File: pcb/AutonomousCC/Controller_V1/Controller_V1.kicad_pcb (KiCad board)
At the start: 2 copper layers, 7 parts, among them J1 Antenna_Conn_02x04_Odd_Even, U1 COM-09032, U2 Pico, U3 COM-09032

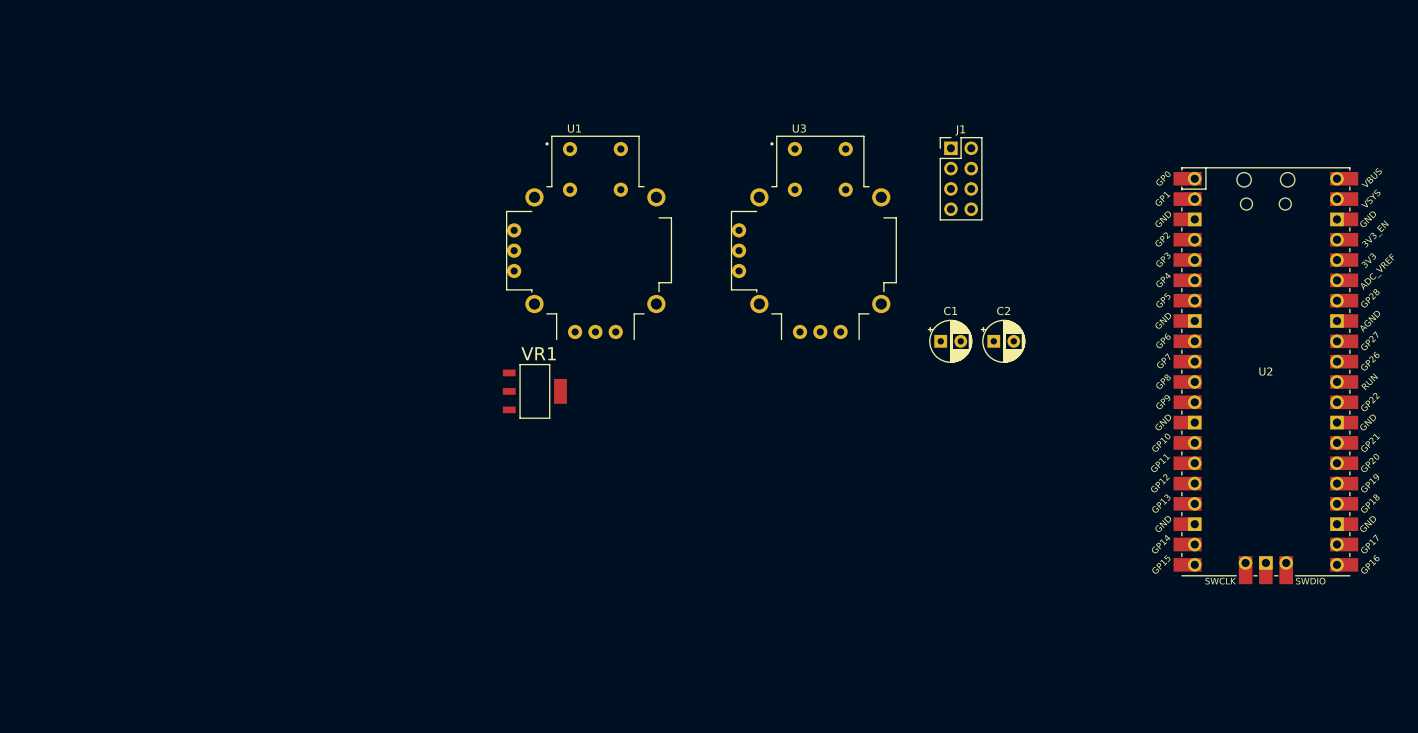
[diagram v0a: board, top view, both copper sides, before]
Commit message: Added USB Port, Button, LED
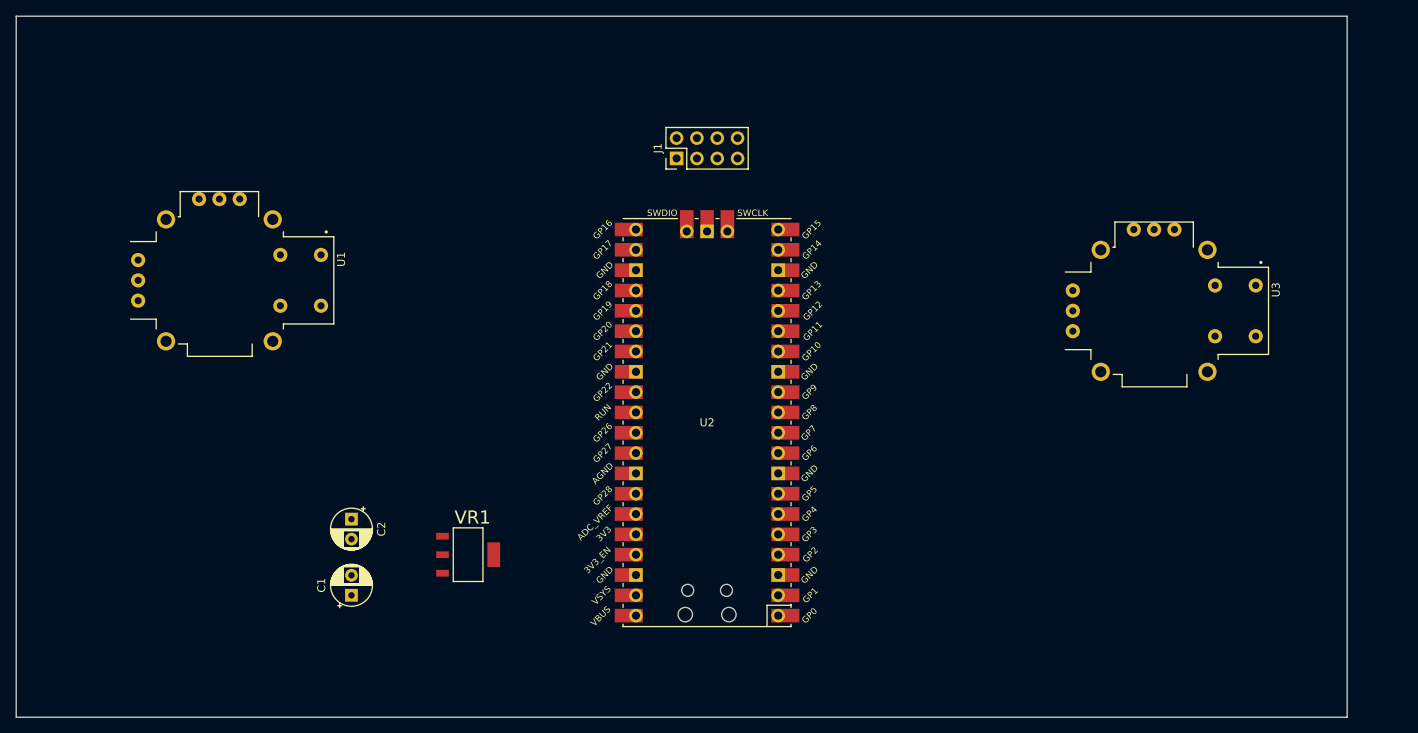
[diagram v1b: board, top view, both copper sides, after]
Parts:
- moved C2 83.3 mm to (118.1, 113.7), turned to 270 degrees
- moved C1 80.2 mm to (118.1, 123.2), turned to 90 degrees
- moved U2 70.1 mm to (162.6, 101.6), turned to 180 degrees
- moved U1 47.2 mm to (101.6, 83.8), turned to 270 degrees
- moved U3 42.4 mm to (218.4, 87.6), turned to 270 degrees
- moved J1 34.3 mm to (158.8, 68.6), turned to 90 degrees
- moved VR1 22.1 mm to (132.7, 118.1)
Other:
- board outline added: 166.4 x 87.6 mm

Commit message: Updated Sch
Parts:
- added J2: USB1130-15-A_REVA, MCU_RaspberryPi_and_Boards:GCT_USB1130-15-A_REVA, F.Cu at (229.9, 61.0)
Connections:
- net Net-(U2-Pad12) renamed GP09
- net Net-(U2-Pad14) renamed GP10
- net Net-(U2-Pad20) renamed GP15
- net Net-(U2-Pad21) renamed GP16

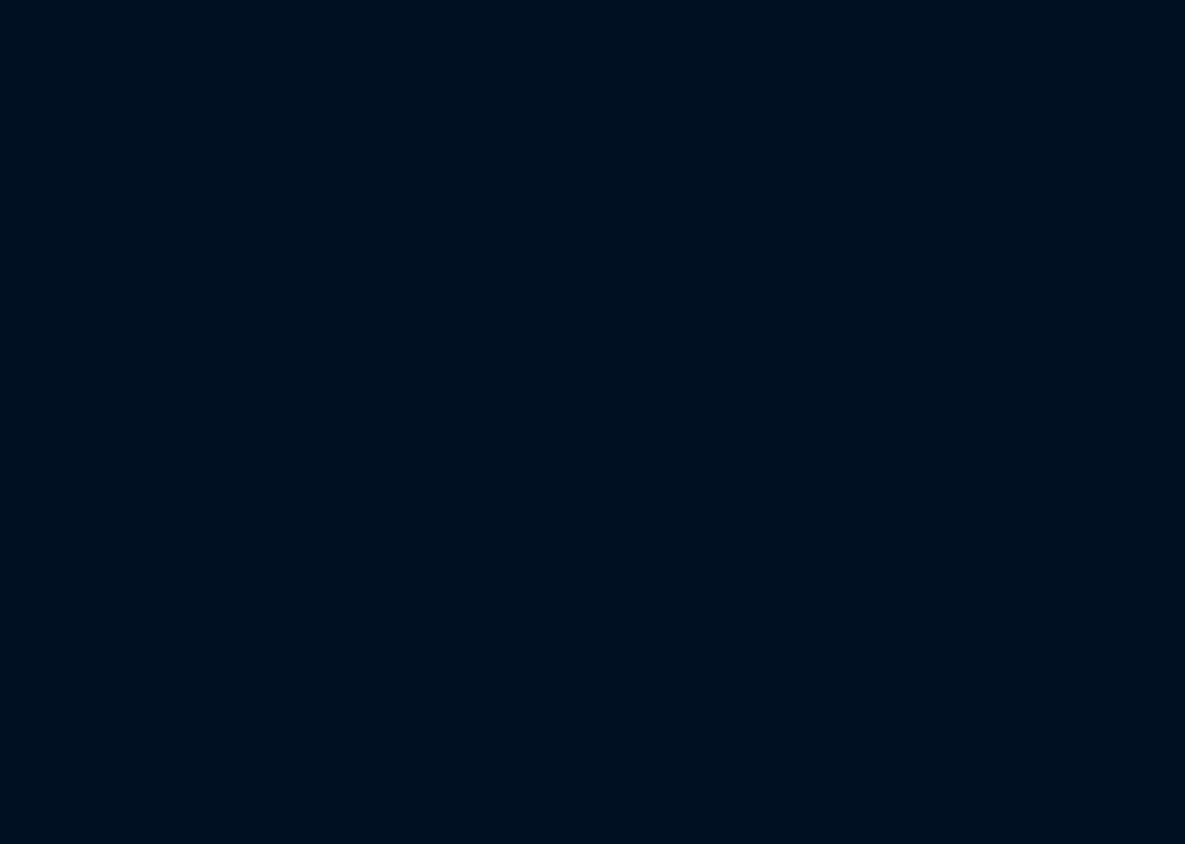
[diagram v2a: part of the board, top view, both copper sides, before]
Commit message: Updated pcb footprints
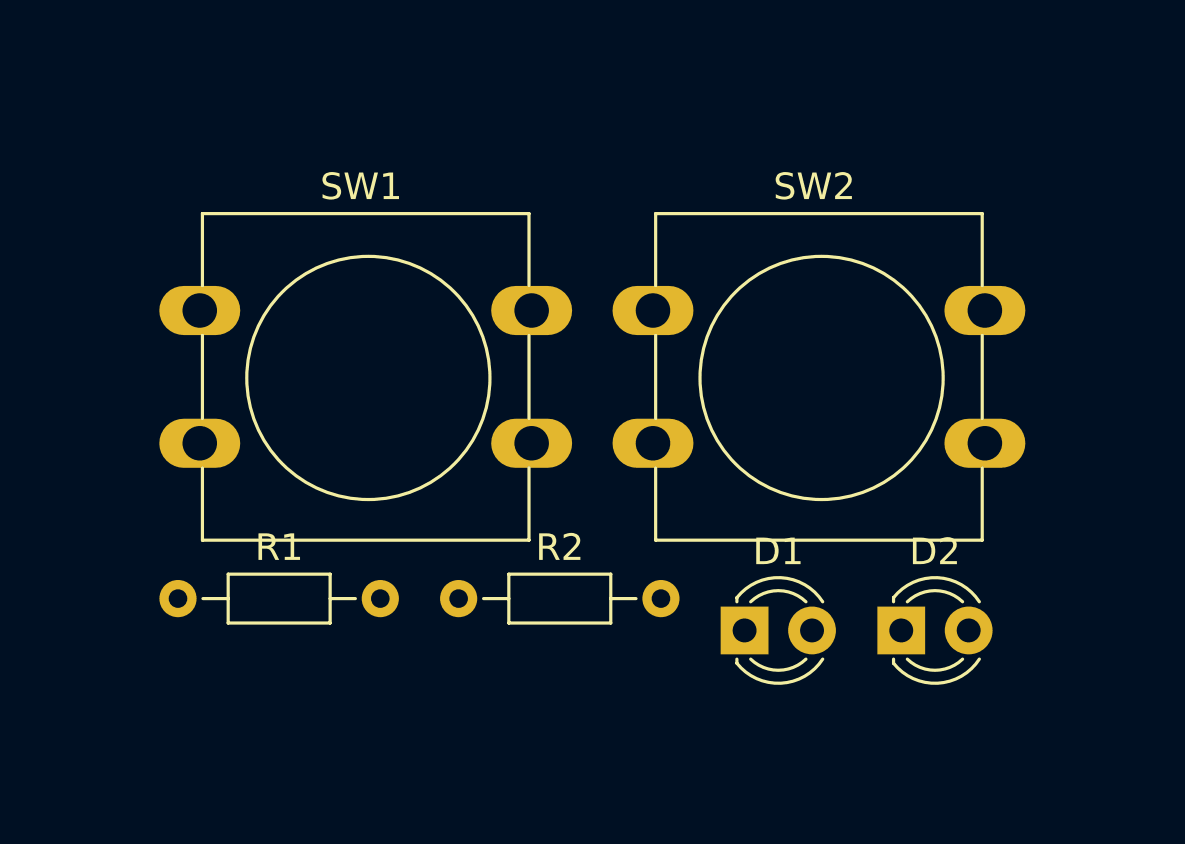
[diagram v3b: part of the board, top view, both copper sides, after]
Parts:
- added D1: Green_LED, LED_THT:LED_D3.0mm, F.Cu at (219.7, 127.0)
- added D2: RED_LED, LED_THT:LED_D3.0mm, F.Cu at (225.6, 127.0)
- added R1: 220_R_Small_US, Resistor_THT:R_Axial_DIN0204_L3.6mm_D1.6mm_P7.62mm_Horizontal, F.Cu at (198.4, 125.8)
- added R2: 220_R_Small_US, Resistor_THT:R_Axial_DIN0204_L3.6mm_D1.6mm_P7.62mm_Horizontal, F.Cu at (208.9, 125.8)
- added SW1: SW_12mm_Push, Button_Switch_THT:SW_PUSH-12mm, F.Cu at (199.2, 115.0)
- added SW2: SW_12mm_Push, Button_Switch_THT:SW_PUSH-12mm, F.Cu at (216.3, 115.0)

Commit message: Updated PCB Layout
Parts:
- added REF**: MountingHole_3.2mm_M3, MountingHole:MountingHole_3.2mm_M3, F.Cu at (106.0, 57.1)
- added REF**: MountingHole_3.2mm_M3, MountingHole:MountingHole_3.2mm_M3, F.Cu at (107.3, 132.7)
- added REF**: MountingHole_3.2mm_M3, MountingHole:MountingHole_3.2mm_M3, F.Cu at (235.6, 132.1)
- added REF**: MountingHole_3.2mm_M3, MountingHole:MountingHole_3.2mm_M3, F.Cu at (236.2, 57.8)
- moved D1 100.6 mm to (148.6, 55.9)
- moved D2 75.8 mm to (199.4, 55.9)
- moved SW1 74.8 mm to (143.1, 65.5)
- moved R1 70.8 mm to (145.4, 78.7)
- moved SW2 54.4 mm to (193.9, 65.4)
- moved R2 46.7 mm to (203.8, 79.4), turned to 180 degrees
- moved C2 23.3 mm to (141.0, 118.1)
- moved C1 23.2 mm to (141.0, 127.0), turned to 270 degrees
- moved U1 21.3 mm to (120.7, 93.3)
- moved U2 13.9 mm to (174.6, 108.6)
- moved J1 12.1 mm to (170.8, 69.2)
- moved J2 7.45 mm to (222.7, 62.9), turned to 180 degrees
- moved VR1 7.41 mm to (128.9, 124.5), turned to 180 degrees
- moved U3 3.70 mm to (220.3, 90.8)
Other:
- board size 166.4 x 87.6 mm -> 142.9 x 87.6 mm
